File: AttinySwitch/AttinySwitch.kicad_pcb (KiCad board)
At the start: 2 copper layers, 45.7 x 24.1 mm, 4 parts, among them IC1 ATTINY84-P, K1 CONN_3, P1 CONN_4X2

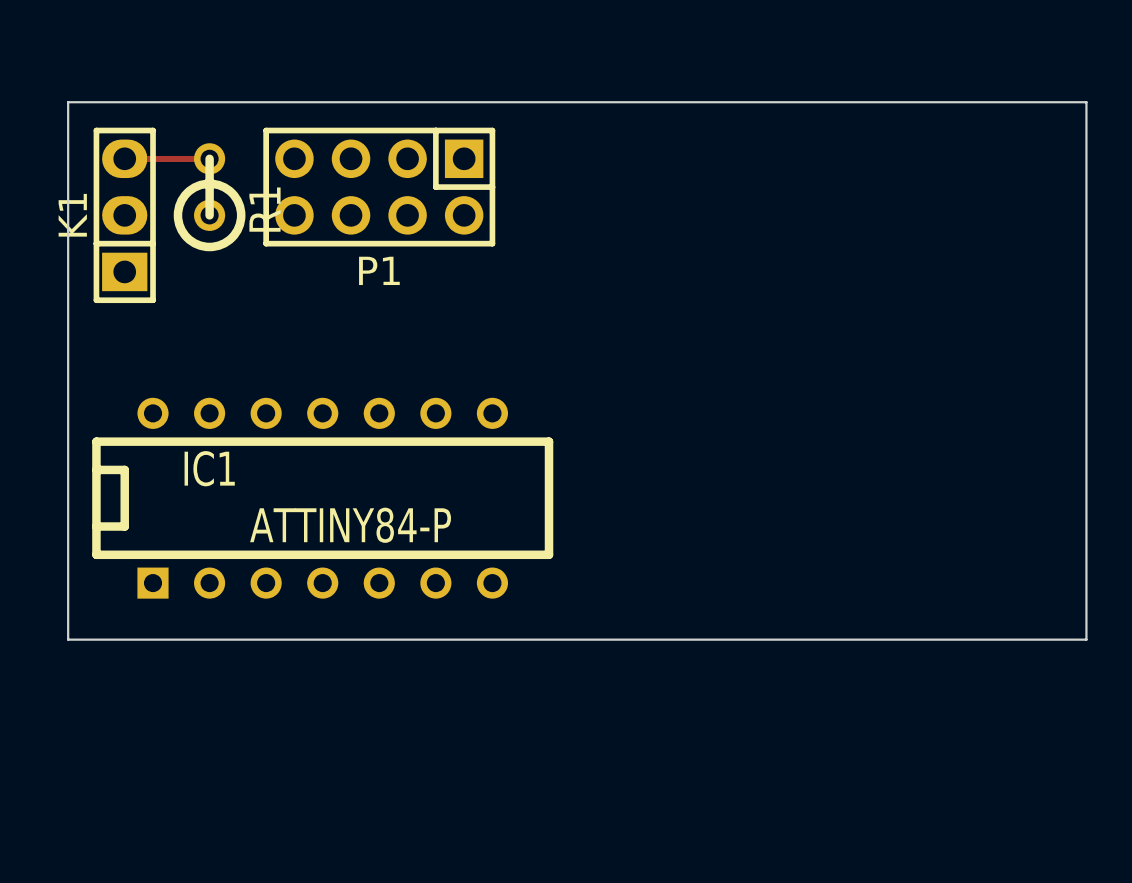
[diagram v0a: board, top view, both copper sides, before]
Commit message: Added voltage regulator and SSR
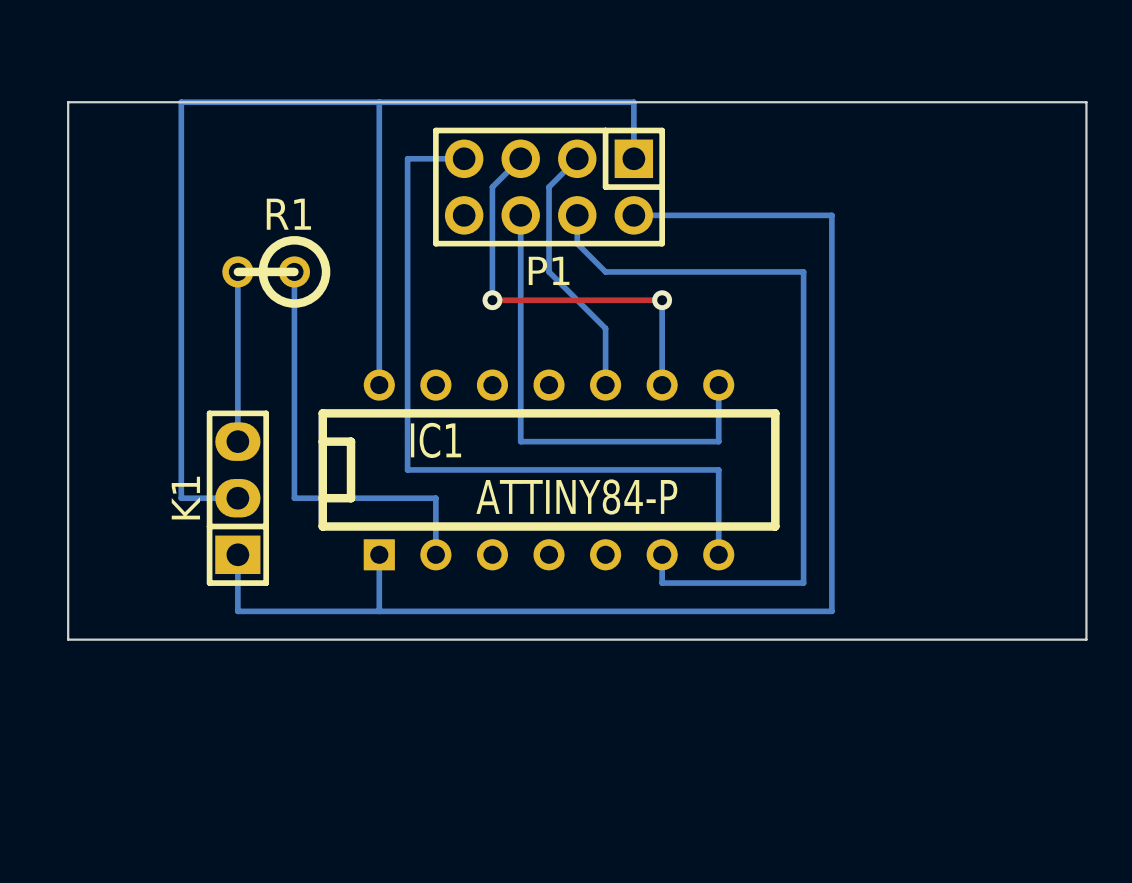
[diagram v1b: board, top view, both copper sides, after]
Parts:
- moved K1 13.7 mm to (71.1, 130.8)
- moved IC1 10.2 mm to (85.1, 129.5)
- moved P1 7.62 mm to (85.1, 116.8)
- moved R1 4.58 mm to (72.4, 120.7), turned to 180 degrees
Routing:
- net Net-(IC1-Pad1): track 0.00 -> 58.4 mm
- net Net-(IC1-Pad14): track 0.00 -> 55.9 mm
- net Net-(IC1-Pad7): track 0.00 -> 34.3 mm
- net Net-(IC1-Pad6): track 0.00 -> 33.5 mm
- net Net-(IC1-Pad8): track 0.00 -> 21.6 mm
- net Net-(IC1-Pad2): track 0.00 -> 19.0 mm
- net Net-(IC1-Pad9): track 0.00 -> 18.3 mm, vias 0 -> 2
- net Net-(IC1-Pad10): track 0.00 -> 11.7 mm
- net Net-(K1-Pad3): track 3.81 -> 7.62 mm

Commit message: Added push button to interrupt pin
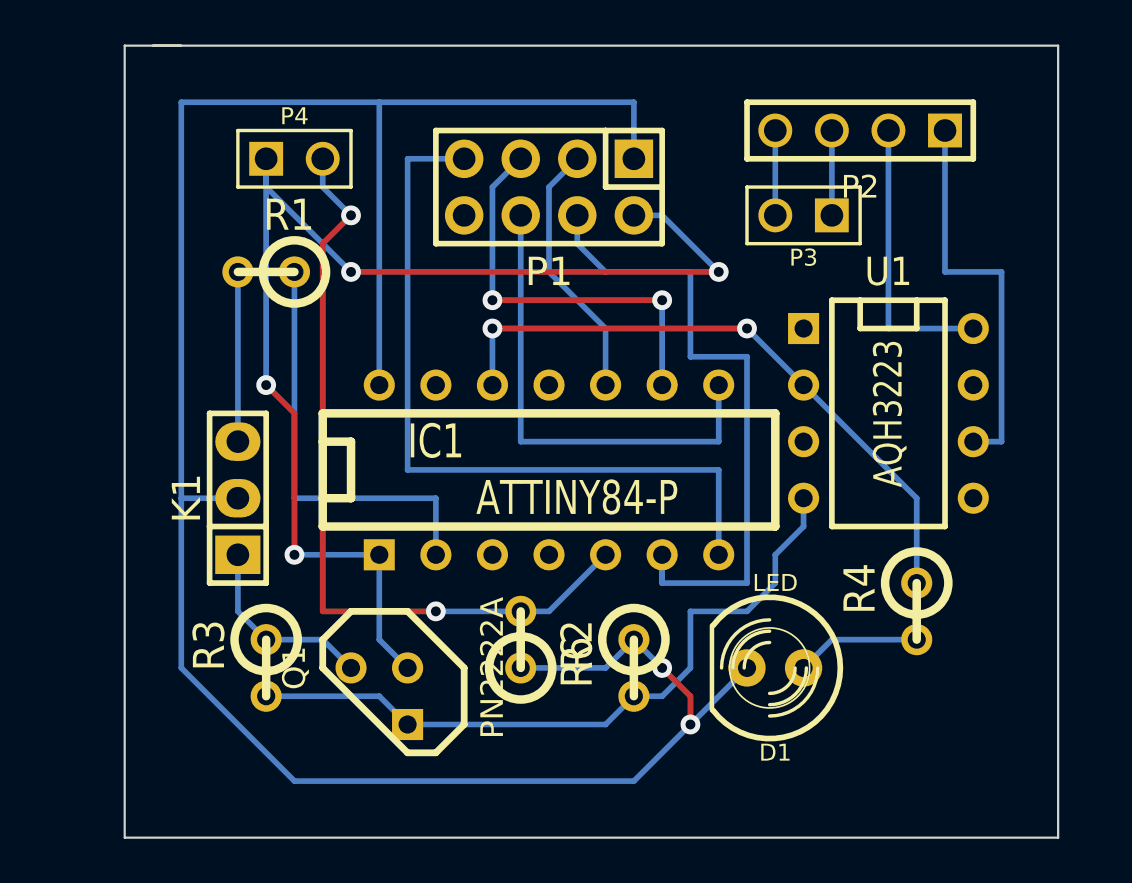
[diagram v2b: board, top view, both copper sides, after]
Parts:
- added D1: LED, LED-5MM, F.Cu at (95.2, 138.4)
- added P2: PWR/LOAD, PIN_ARRAY_4x1, F.Cu at (99.1, 114.3)
- added P3: CONN_2, PIN_ARRAY_2X1, F.Cu at (96.5, 118.1)
- added P4: SWITCH, PIN_ARRAY_2X1, F.Cu at (73.7, 115.6)
- added Q1: PN2222A, TO92, F.Cu at (77.5, 139.7)
- added R2: 10K, R1, F.Cu at (88.9, 138.4)
- added R3: 1K, R1, F.Cu at (72.4, 138.4)
- added R4: 220, R1, F.Cu at (101.6, 135.9)
- added R6: 100K, R1, F.Cu at (83.8, 137.2)
- added U1: AQH3223, DIP-8__300, F.Cu at (100.3, 127.0)
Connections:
- net Net-(IC1-Pad14) renamed /GND
- IC1 pad 1: Net-(IC1-Pad1) -> N-0000020
- IC1 pad 11: Net-(IC1-Pad11) -> (no net)
- IC1 pad 13: Net-(IC1-Pad13) -> (no net)
- IC1 pad 3: Net-(IC1-Pad3) -> (no net)
- IC1 pad 4: Net-(IC1-Pad4) -> (no net)
- K1 pad 1: Net-(IC1-Pad1) -> /+5v
- P1 pad 5: Net-(P1-Pad5) -> (no net)
- P1 pad 8: Net-(IC1-Pad1) -> N-0000020
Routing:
- net Net-(IC1-Pad1): track 58.4 -> 0.00 mm
- net N-0000020: track 0.00 -> 55.8 mm, vias 0 -> 4
- net /GND: track 55.9 -> 103.6 mm, vias 0 -> 2
- net N-0000016: track 0.00 -> 35.1 mm, vias 0 -> 2
- net N-0000010: track 0.00 -> 31.8 mm
- net N-0000012: track 0.00 -> 28.6 mm, vias 0 -> 2
- net N-0000023: track 0.00 -> 17.8 mm
- net N-0000019: track 0.00 -> 12.7 mm
- net /+5v: track 0.00 -> 8.67 mm
- net N-000003: track 0.00 -> 5.61 mm
- net N-0000022: track 0.00 -> 3.81 mm
- net N-0000021: track 0.00 -> 3.81 mm
- net N-000004: track 33.5 -> 29.7 mm
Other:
- board size 45.7 x 24.1 mm -> 41.9 x 35.6 mm
